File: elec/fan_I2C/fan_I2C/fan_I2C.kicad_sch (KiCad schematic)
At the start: 2 parts, among them J101 DB9_Female_MountingHoles, J102 DB25_Female_MountingHoles

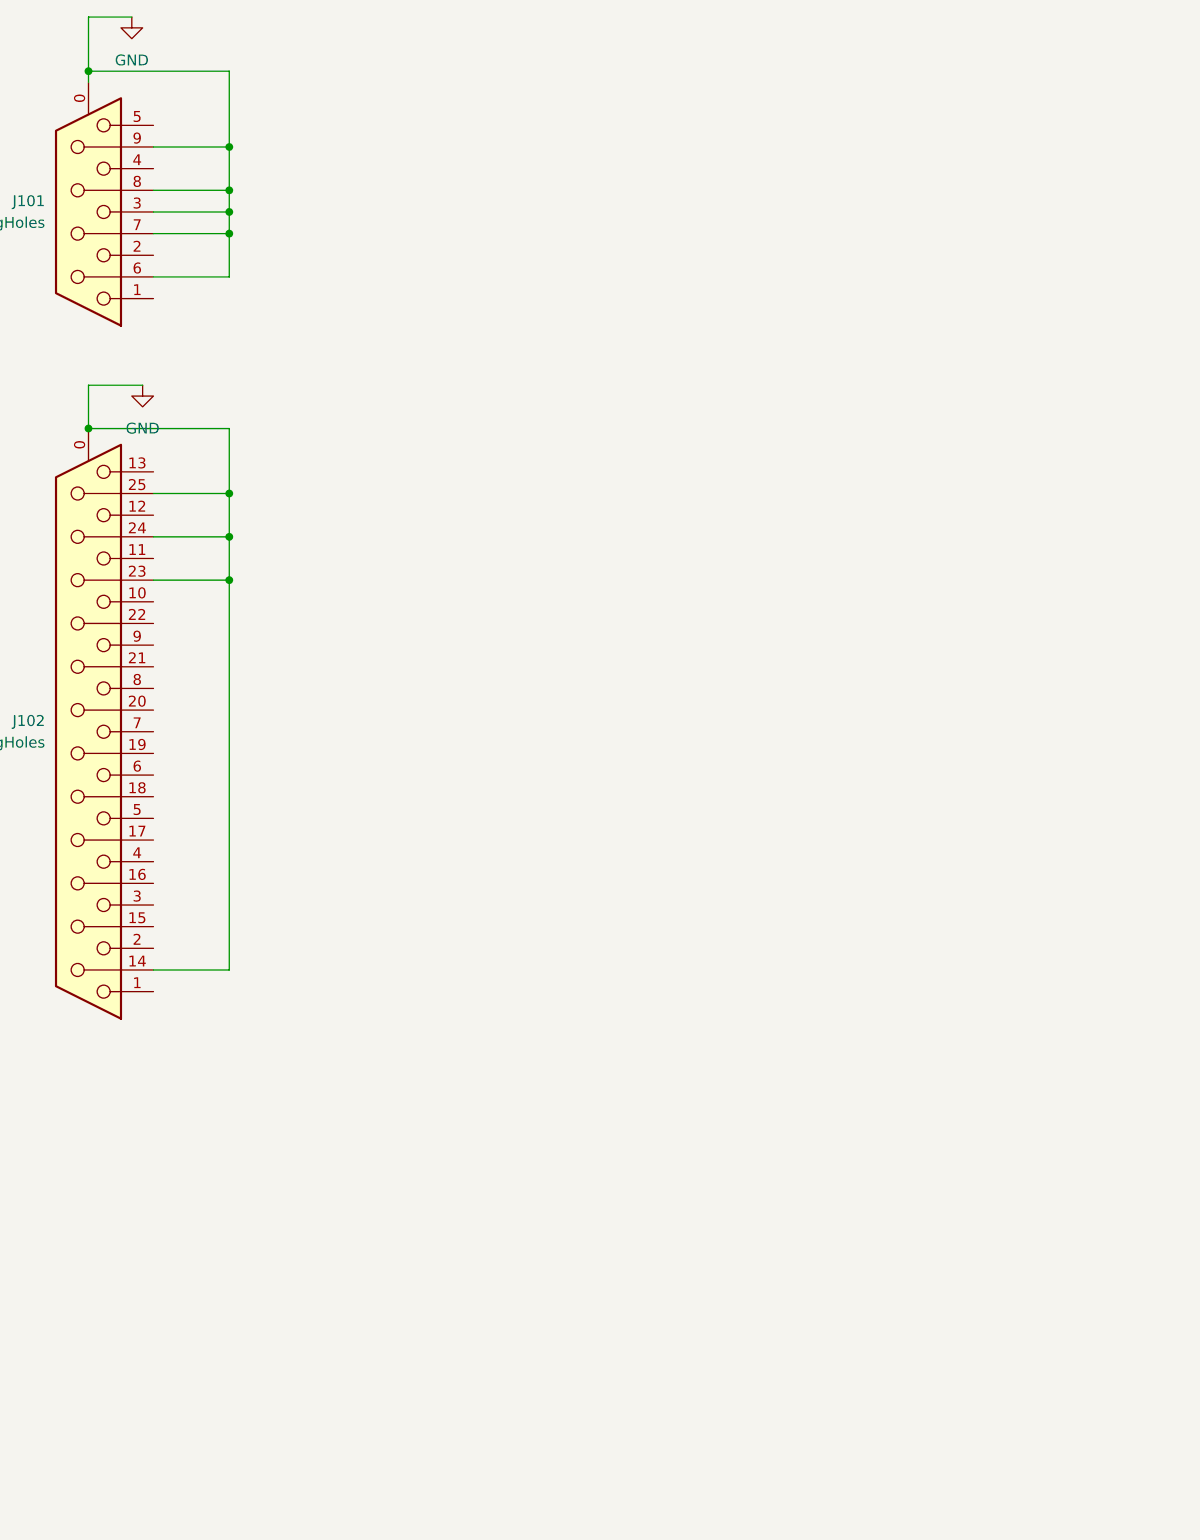
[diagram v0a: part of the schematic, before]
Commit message: Add SPI and I2C level shifter circuits lifted from the PolyVent Interface Card.
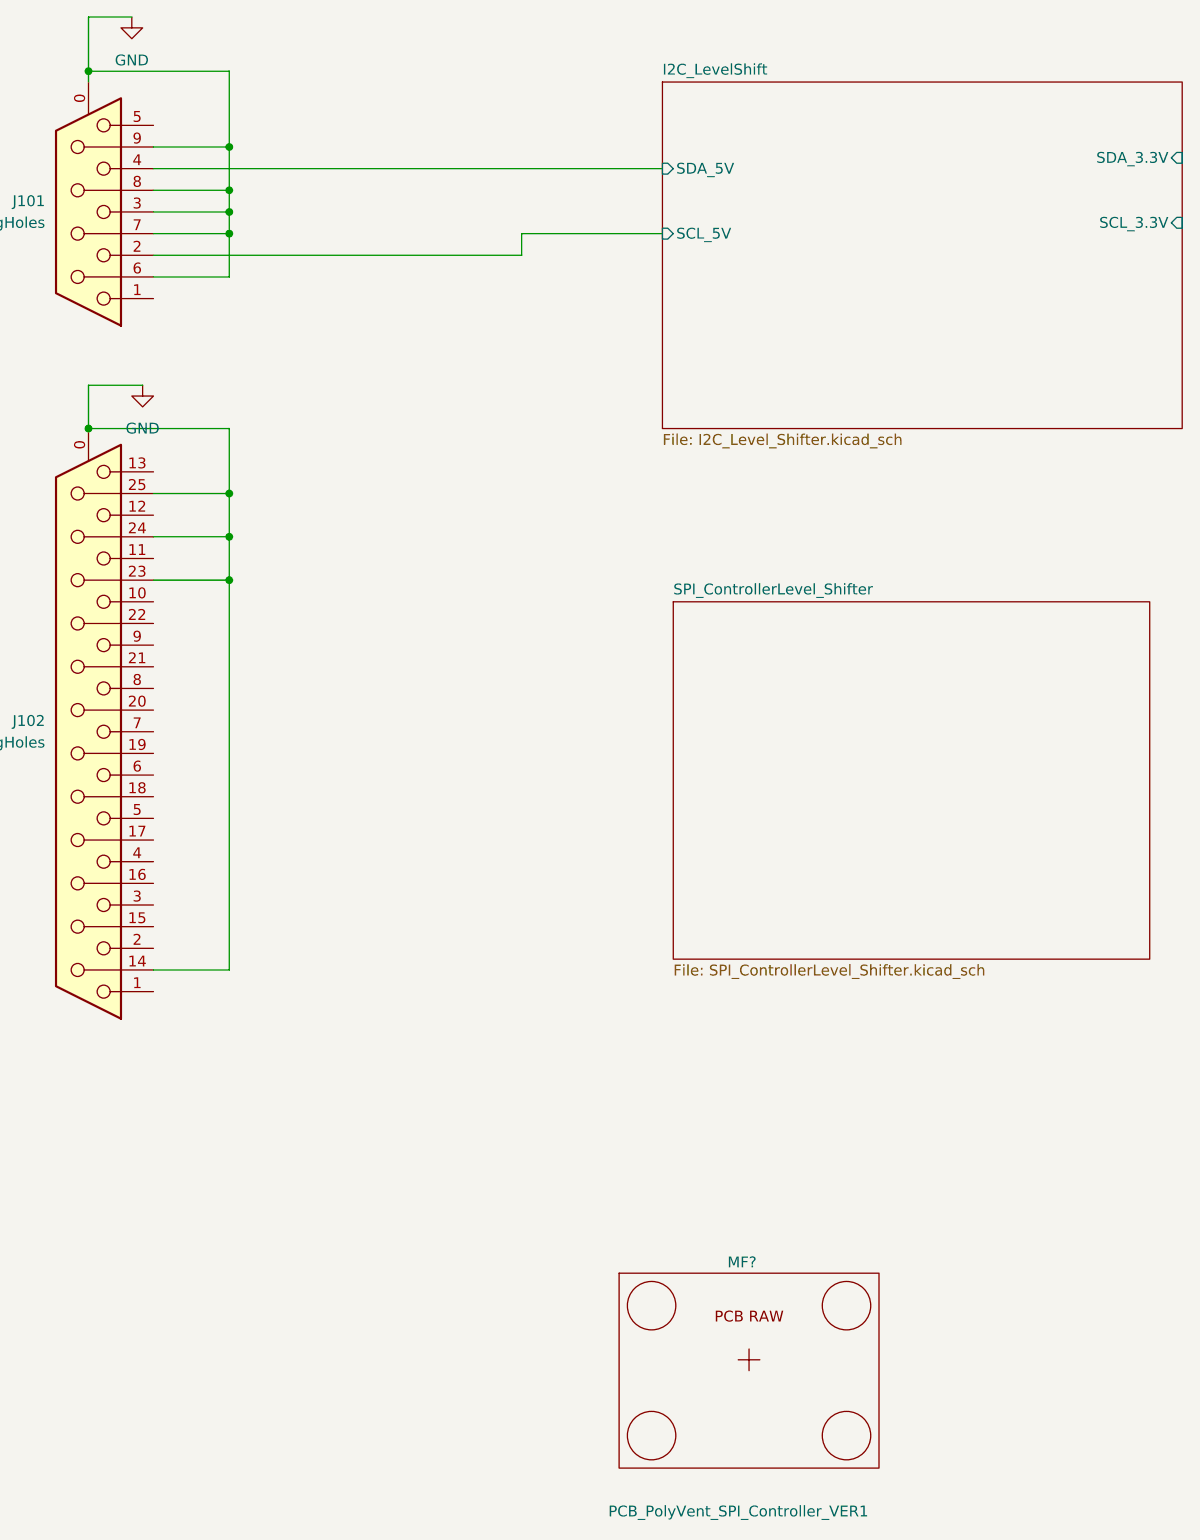
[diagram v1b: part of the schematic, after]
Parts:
- added MF?: PCB_PolyVent_SPI_Controller_VER1, NA, symbol GPAD_SCH_LIB:PCB_GPAD_VER1
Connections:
- net I2C_LevelShift/SCL_5V: now reaches J101.2
- net I2C_LevelShift/SDA_5V: now reaches J101.4
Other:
- added sheet I2C_LevelShift (I2C_Level_Shifter.kicad_sch)
- added sheet SPI_ControllerLevel_Shifter (SPI_ControllerLevel_Shifter.kicad_sch)
- title: fan_I2C -> SPI 3V3 to 5V Controller Interface

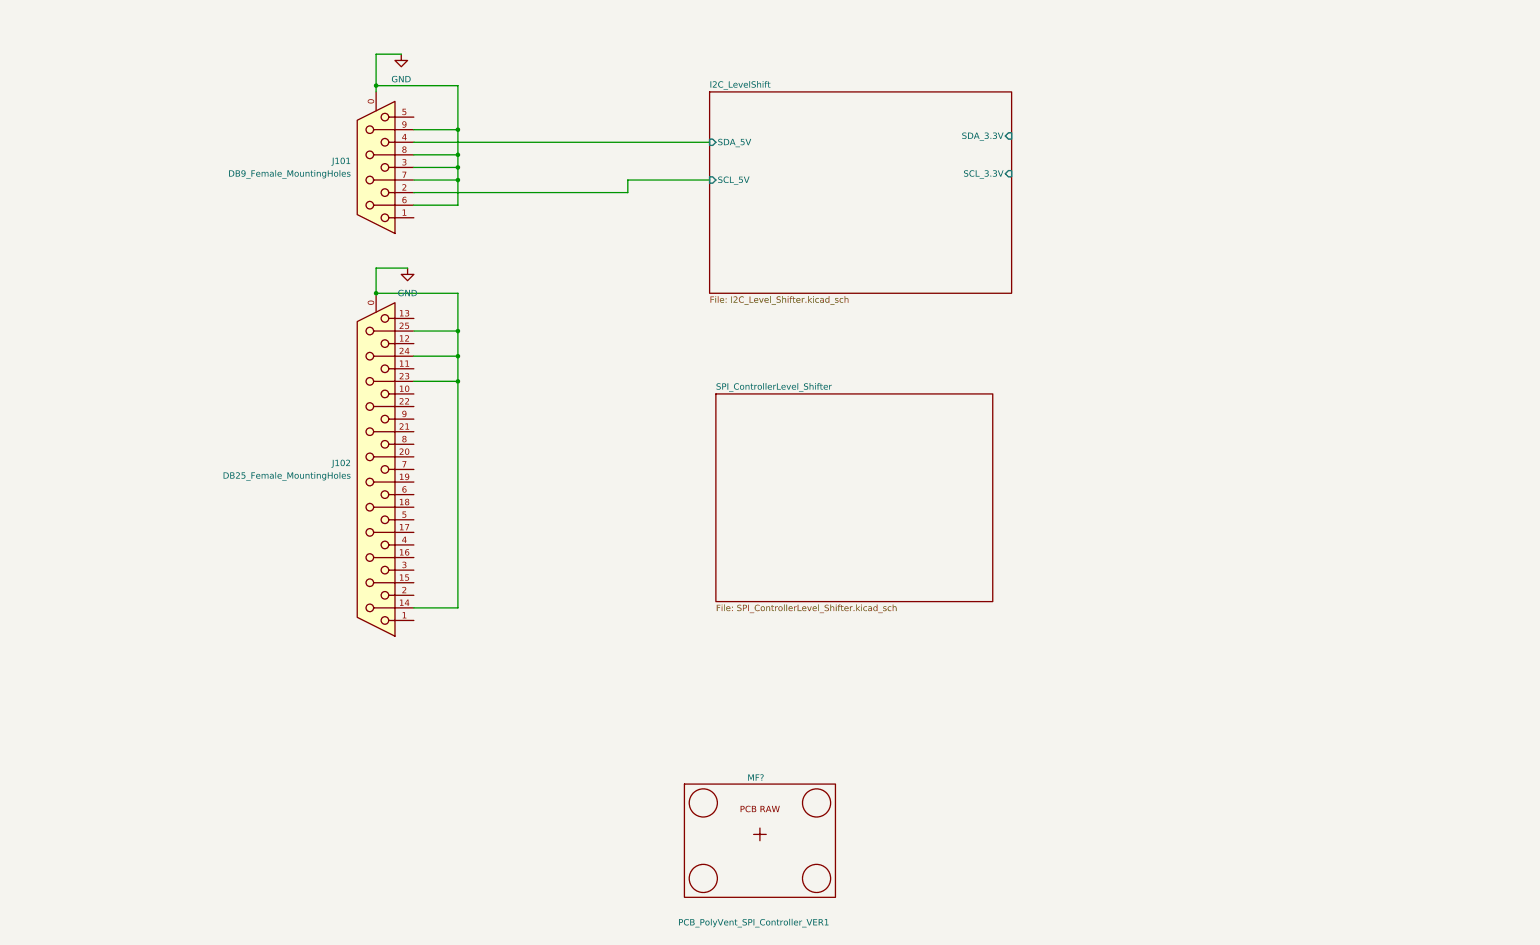
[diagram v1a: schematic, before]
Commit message: Making power local to the sheets.
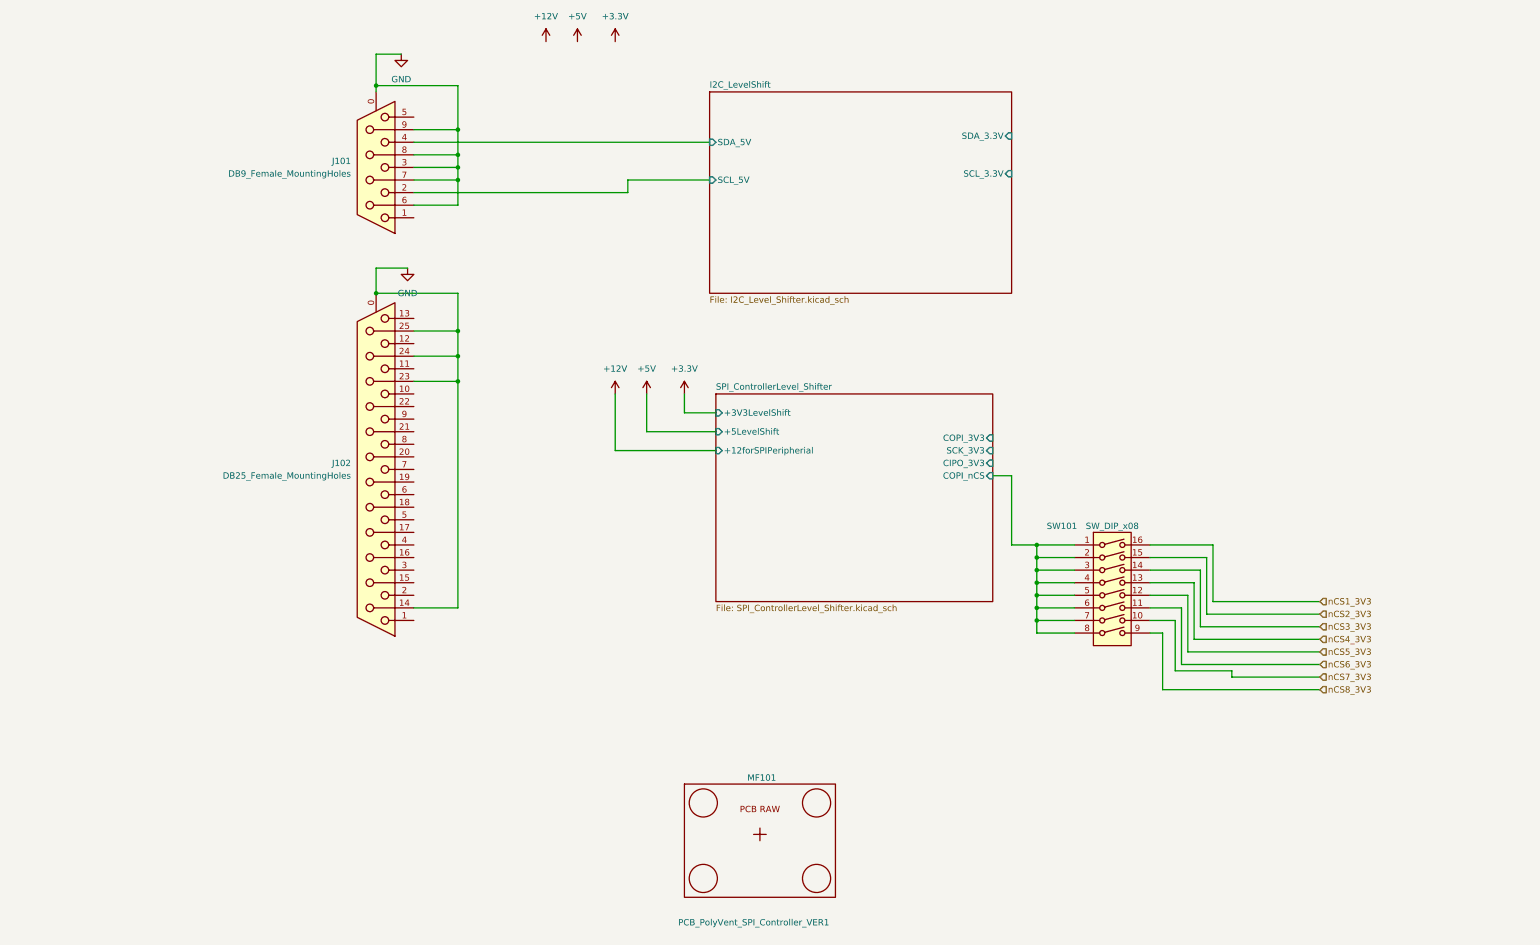
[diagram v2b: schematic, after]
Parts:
- added SW101: SW_DIP_x08, PubInv_PCB:SMDIP-16_L11.39_W6.7mm, symbol Switch:SW_DIP_x08
- gave numbers to parts that had none: 1
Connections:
- new net SPI_ControllerLevel_Shifter/COPI_nCS: SW101.1, SW101.2, SW101.3, SW101.4, SW101.5, SW101.6, SW101.7, SW101.8
- new net nCS1_3V3: SW101.16
- new net nCS2_3V3: SW101.15
- new net nCS3_3V3: SW101.14
- new net nCS4_3V3: SW101.13
- new net nCS5_3V3: SW101.12
- new net nCS6_3V3: SW101.11
- new net nCS7_3V3: SW101.10
- new net nCS8_3V3: SW101.9
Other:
- sheet SPI_ControllerLevel_Shifter ports: added +12forSPIPeripherial, +3V3LevelShift, +5LevelShift, CIPO_3V3, COPI_3V3, COPI_nCS, SCK_3V3; removed none

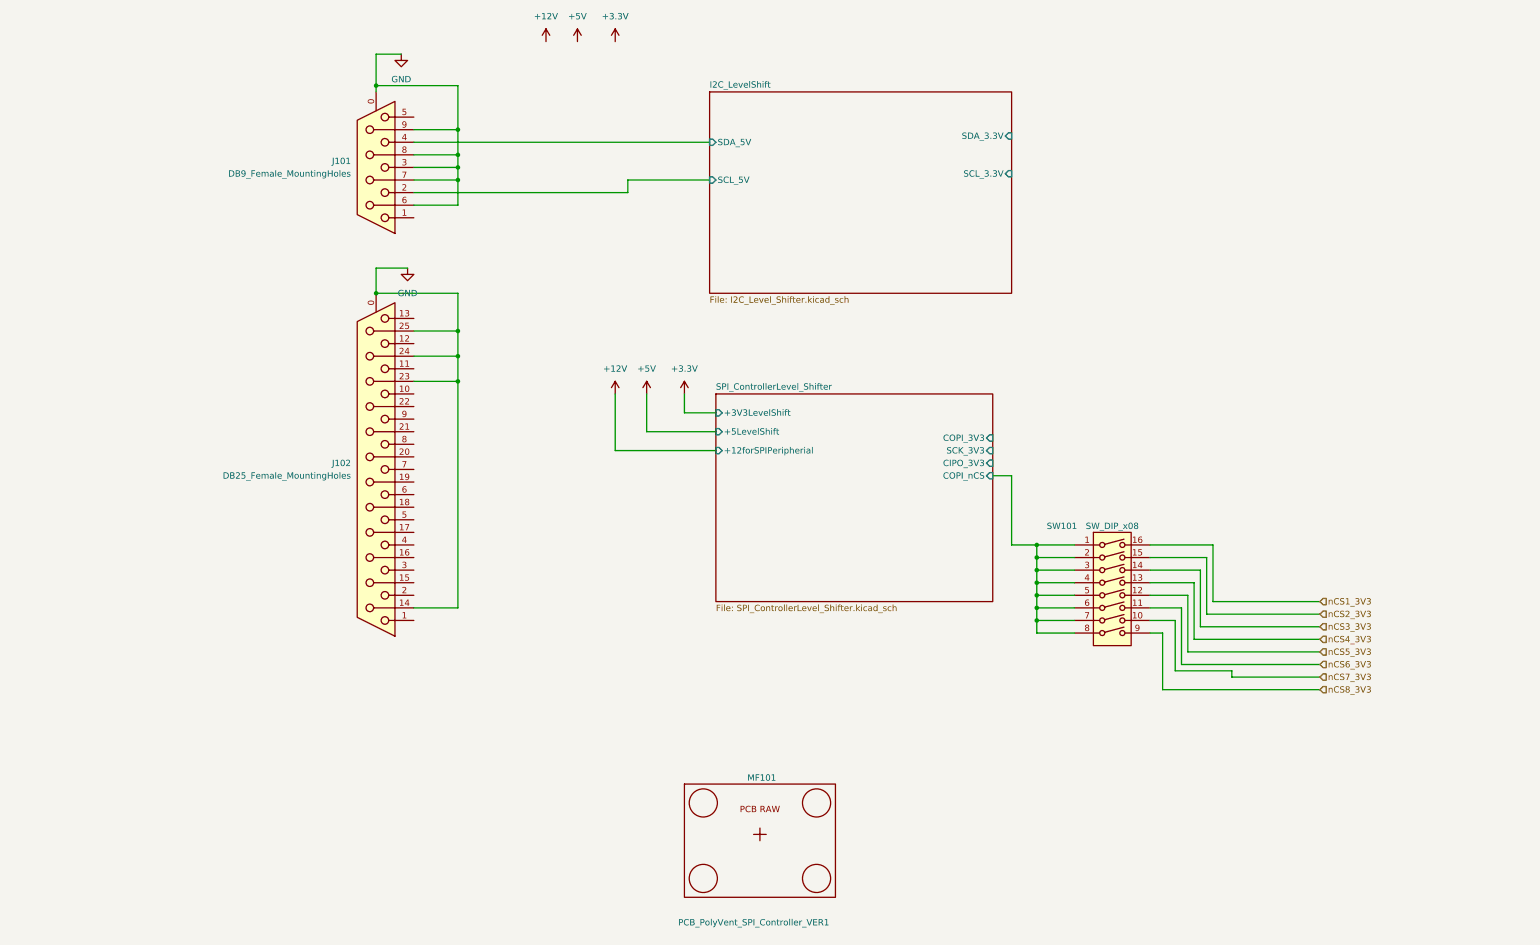
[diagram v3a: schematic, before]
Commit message: Add Connectors like Roberts Fritzing.
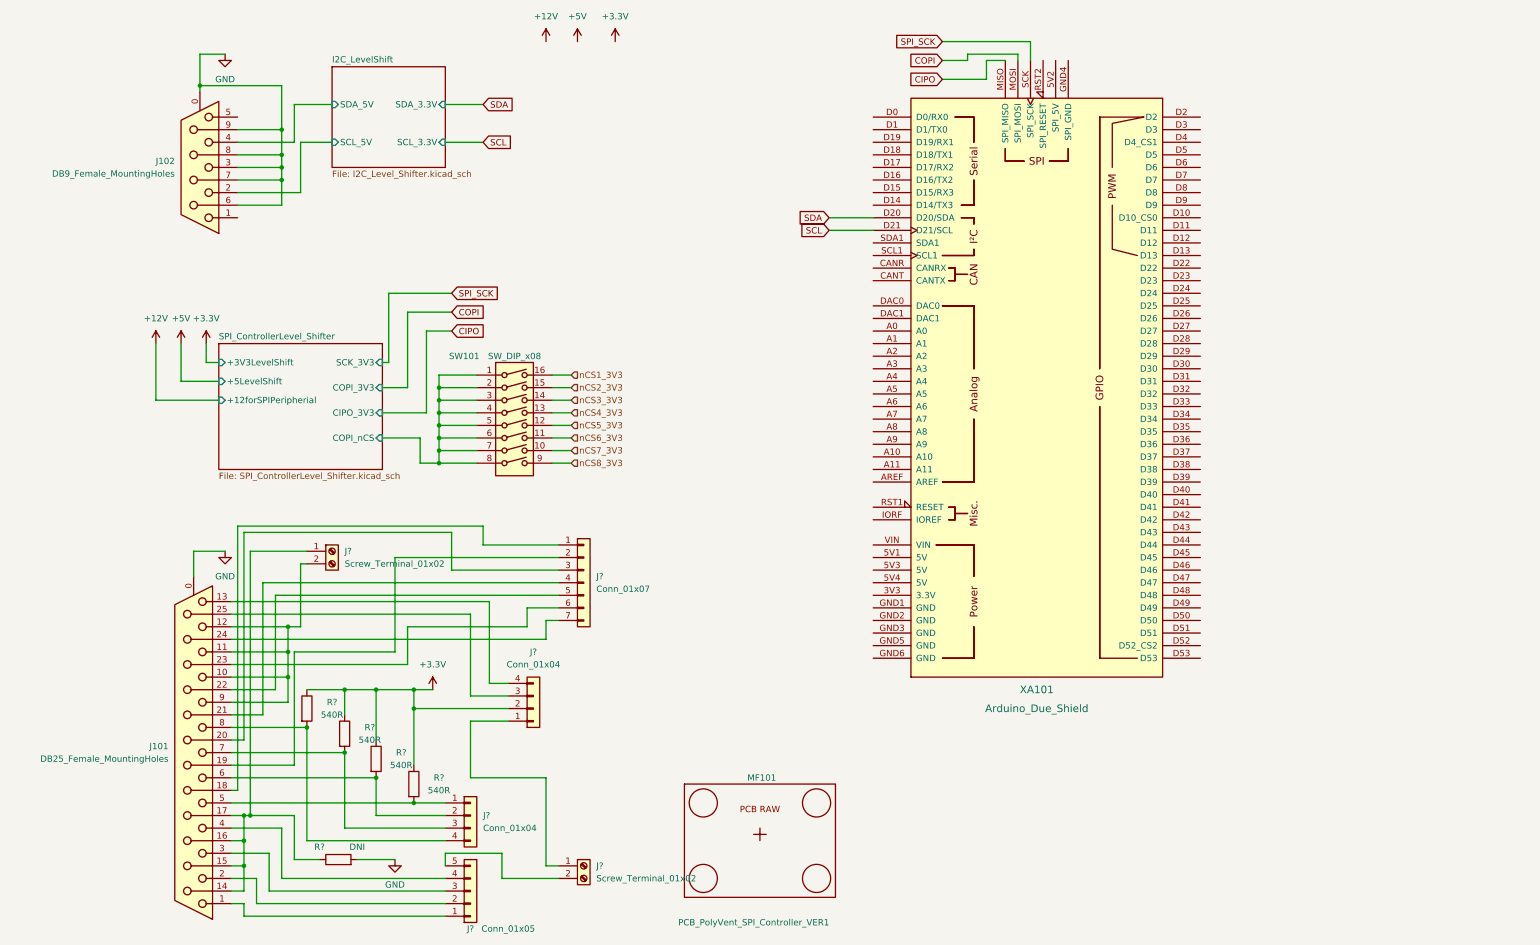
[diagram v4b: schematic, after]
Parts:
- added J?: Conn_01x05, Connector_PinHeader_2.54mm:PinHeader_1x05_P2.54mm_Vertical, symbol Connector_Generic:Conn_01x05
- added J? (x2): Screw_Terminal_01x02, symbol Connector:Screw_Terminal_01x02
- added J? (x2): Conn_01x04, Connector_PinHeader_2.54mm:PinHeader_1x04_P2.54mm_Vertical, symbol Connector_Generic:Conn_01x04
- added J?: Conn_01x07, Connector_PinHeader_2.54mm:PinHeader_1x07_P2.54mm_Vertical, symbol Connector_Generic:Conn_01x07
- added R? (x4): 540R, Resistor_SMD:R_0603_1608Metric_Pad0.98x0.95mm_HandSolder, symbol Device:R
- added R?: DNI, Resistor_SMD:R_0603_1608Metric_Pad0.98x0.95mm_HandSolder, symbol Device:R
- added XA101: Arduino_Due_Shield, arduino-library:Arduino_Due_Shield, symbol arduino-library:Arduino_Due_Shield
- renumbered J102 to J101, J101 to J102
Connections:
- net +3.3V: now also J?.2 (Pin_2), R?.1, R?.1, R?.1, R?.1
- net GND: now also R?.2; no longer J101.14 (P14), J101.23 (P23), J101.24 (P24), J101.25 (P25)
- net at J101.1: now also J?.1 (Pin_1)
- net at J101.10: now also J101.11, J101.12, J101.9, J?.2 (Pin_2)
- net at J101.13: now also J?.4 (Pin_4)
- net at J101.15 (P15): now also J101.14 (P14), J101.16 (P16), J101.17 (P17), J?.1 (Pin_1), R?.1
- net at J101.18 (P18): now also J?.1 (Pin_1)
- net at J101.19 (P19): now also J?.2 (Pin_2)
- net at J101.2: now also J?.2 (Pin_2)
- net at J101.20 (P20): now also J?.3 (Pin_3)
- net at J101.21 (P21): now also J?.4 (Pin_4)
- net at J101.22 (P22): now also J?.5 (Pin_5)
- net at J101.3: now also J?.3 (Pin_3)
- net at J101.4: now also J?.4 (Pin_4)
- net at J101.5: now also J?.1 (Pin_1), R?.2
- net at J101.6: now also J?.2 (Pin_2), R?.2
- net at J101.7: now also J?.3 (Pin_3), R?.2
- net at J101.8: now also J?.4 (Pin_4), R?.2
- new net: J101.23 (P23), J?.6 (Pin_6)
- new net: J101.24 (P24), J?.7 (Pin_7)
- new net: J101.25 (P25), J?.3 (Pin_3)
- new net: J?.2 (Pin_2), J?.5 (Pin_5)
- new net: J?.1 (Pin_1), J?.1 (Pin_1)
- new net CIPO: XA101.MISO (SPI_MISO)
- new net COPI: XA101.MOSI (SPI_MOSI)
- new net SCL: XA101.D21 (D21/SCL)
- new net SDA: XA101.D20 (D20/SDA)
- new net SPI_SCK: XA101.SCK (SPI_SCK)
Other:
- moved on the sheet: J101, J102, SW101
